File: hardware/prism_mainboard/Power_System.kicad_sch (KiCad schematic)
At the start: 32 parts, among them U3 LP873222RHDRQ1, U4 100uF, U5 0.47uF, U6 4.7uF, U7 GND

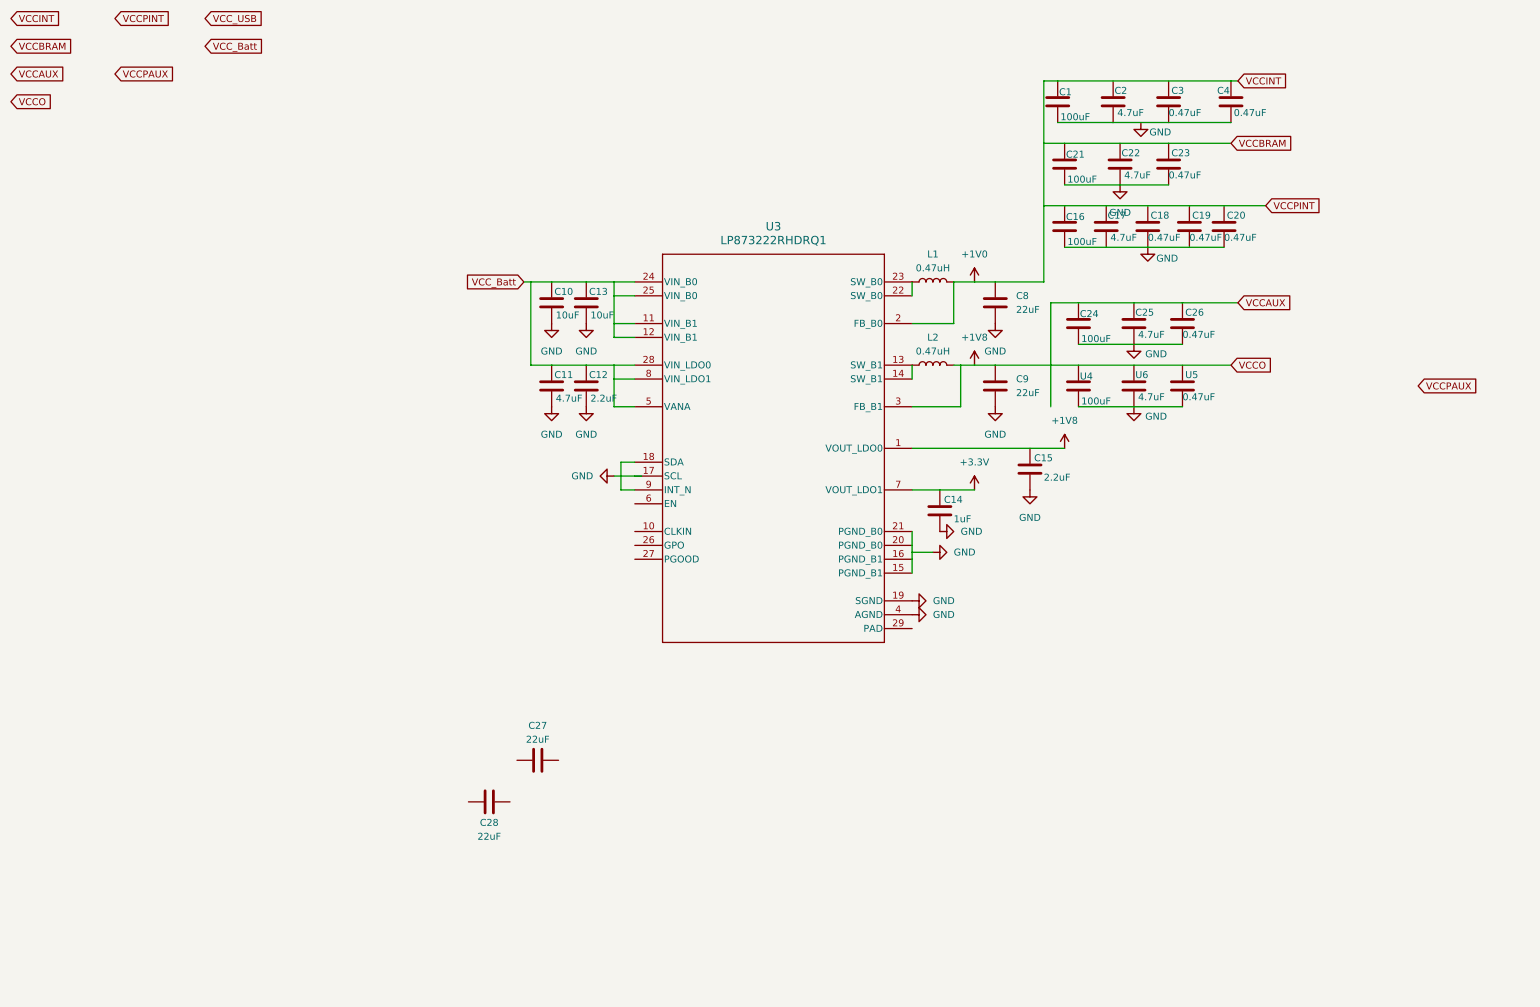
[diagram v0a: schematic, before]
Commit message: Power System Schematics
Updated Power System Schematics, changed the power supply IC from 2 Buck 2 LDO to 4 Buck and include 2 LDO to provide Low Noise power to RF and sensitive circuitry
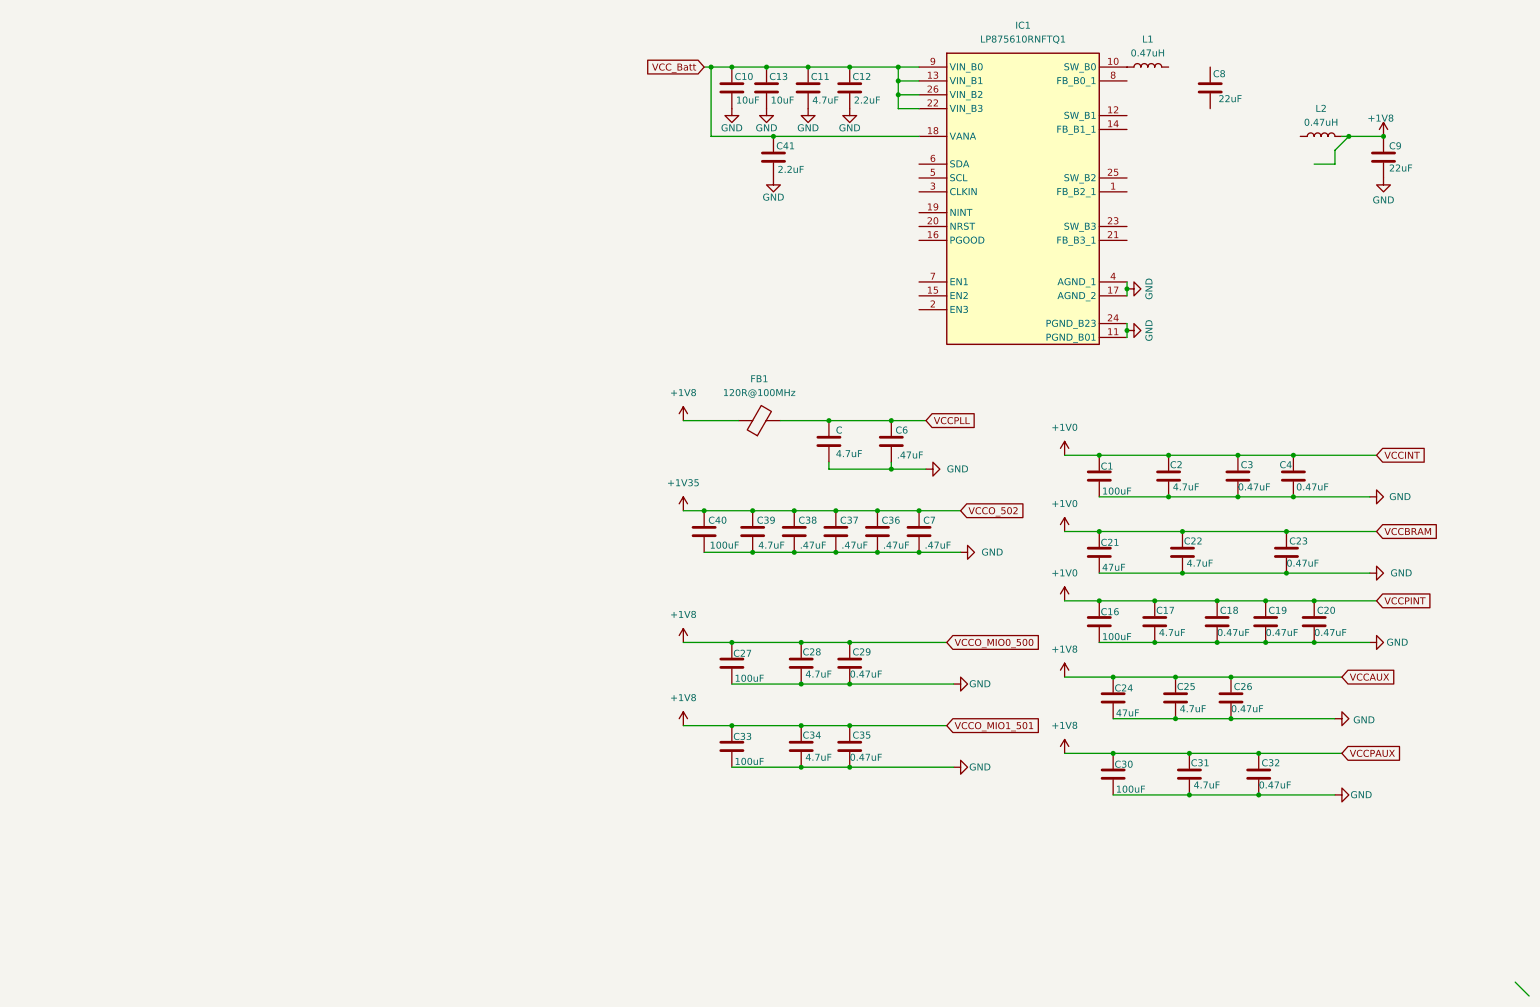
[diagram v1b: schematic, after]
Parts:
- removed C14: 1uF, Capacitor_SMD:C_0201_0603Metric, symbol Device:C
- removed C15: 2.2uF, Capacitor_SMD:C_0201_0603Metric, symbol Device:C
- removed U3: LP873222RHDRQ1, RHD0028W, symbol 2026-05-18_00-35-41:LP873222RHDRQ1
- removed U4: 100uF, symbol Device:C
- removed U5: 0.47uF, symbol Device:C
- removed U6: 4.7uF, symbol Device:C
- removed U7: GND, symbol power:GND
- added C, C31, C34, C39: 4.7uF, Capacitor_SMD:C_0805_2012Metric, symbol Device:C
- added C29, C32, C35: 0.47uF, symbol Device:C
- added C30, C33, C40: 100uF, Capacitor_SMD:C_1210_3225Metric, symbol Device:C
- added C36, C37, C38, C6, C7: .47uF, symbol Device:C
- added C41: 2.2uF, Capacitor_SMD:C_0201_0603Metric, symbol Device:C
- added FB1: 120R@100MHz, symbol Device:FerriteBead
- added IC1: LP875610RNFTQ1, LP87524TRNFRQ1, symbol SamacSys:LP875610RNFTQ1
- C1, C16: footprint (none) -> Capacitor_SMD:C_1210_3225Metric; Protoflow_Source kicad -> (none)
- C10, C11, C12, C13, C18, C19, C20, C23, C26, C3, C4, C8, C9, L1, L2: Protoflow_Source kicad -> (none)
- C17, C2, C22, C25: footprint (none) -> Capacitor_SMD:C_0805_2012Metric; Protoflow_Source kicad -> (none)
- C21, C24: value 100uF -> 47uF; footprint (none) -> Capacitor_SMD:C_1210_3225Metric; Protoflow_Source kicad -> (none)
- C27: value 22uF -> 100uF; footprint ProtoFlow.pretty:C0805 -> Capacitor_SMD:C_1210_3225Metric; FastEDA_CatalogStatus noExactMatch -> (none); FastEDA_Package 0805 -> (none); FastEDA_StatusMessage No exact part available for 22uF 50V 0805. -> (none); FastEDA_Voltage 50V -> (none); Protoflow_Source native -> (none)
- C28: value 22uF -> 4.7uF; footprint ProtoFlow.pretty:C0805 -> Capacitor_SMD:C_0805_2012Metric; FastEDA_CatalogStatus noExactMatch -> (none); FastEDA_Package 0805 -> (none); FastEDA_StatusMessage No exact part available for 22uF 50V 0805. -> (none); FastEDA_Voltage 50V -> (none); Protoflow_Source native -> (none)
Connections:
- net VCCAUX is gone; now on net +1V8: C24.1, C25.1, C26.1, C9.1, L2.2
- net VCC_Batt: now also C41.1, IC1.13 (VIN_B1), IC1.18 (VANA), IC1.22 (VIN_B3), IC1.26 (VIN_B2), IC1.9 (VIN_B0)
- net GND: now reaches C16.2, C17.2, C18.2, C19.2, C20.2
- net GND: now also C1.2, C10.2, C11.2, C12.2, C13.2, C2.2, C21.2, C22.2, C23.2, C24.2, C25.2, C26.2, C27.2, C28.2, C3.2, C4.2, C9.2, C.2, C29.2, C30.2, C31.2, C32.2, C33.2, C34.2, C35.2, C36.2, C37.2, C38.2, C39.2, C40.2, C41.2, C6.2, C7.2, IC1.11 (PGND_B01), IC1.17 (AGND_2), IC1.24 (PGND_B23), IC1.4 (AGND_1)
- net +1V0: now reaches C2.1
- net +1V0: now also C1.1, C16.1, C17.1, C18.1, C19.1, C20.1, C21.1, C22.1, C23.1, C3.1, C4.1
- net +1V8: now reaches C27.1
- net +1V8: now also C28.1, C29.1, C30.1, C31.1, C32.1, C33.1, C34.1, C35.1, FB1.1
- net at L1.1: now also IC1.10 (SW_B0)
- removed net VCCBRAM: C1.1, C16.1, C17.1, C18.1, C19.1, C20.1, C21.1, C22.1, C23.1, C4.1, C8.1, L1.2
- new net +1V35: C36.1, C37.1, C38.1, C39.1, C40.1, C7.1
- new net VCCPLL: C.1, C6.1, FB1.2
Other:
- company: Protoflow -> (none)
- title: Untitled -> (none)
